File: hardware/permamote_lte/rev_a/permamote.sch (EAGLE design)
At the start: 115 parts, among them IC1 NRF9160, J1 TC2030-JLINK-NL, J2 U.FL-R-SMT, J3 NANO_SIM, J4 U.FL-R-SMT, J5 DM3AT-SF-PEJM5, Q1 PMDXB950UPEL, Q10 PMDXB950UPEL, Q2 PMDXB950UPEL, Q3 PMDXB950UPEL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

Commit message: cleaned up wirestubs
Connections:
- net GND: now also U13.EPAD
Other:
- moved on the sheet: TP30, TP31
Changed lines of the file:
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@@
 <part name="GND40" library="supply1" library_urn="urn:adsk.eagle:library:371" deviceset="GND" device=""/>
 <part name="P+13" library="supply1" library_urn="urn:adsk.eagle:library:371" deviceset="VCC" device=""/>
+<part name="GND41" library="umich" deviceset="GND" device=""/>
 </parts>
 <sheets>
@@
 <attribute name="AUTHOR" x="169.545" y="6.35" size="2.54" layer="94" font="vector"/>
 </instance>
-<instance part="TP30" gate="G$1" x="50.8" y="124.46" smashed="yes" rot="R270">
-<attribute name="NAME" x="50.8" y="127.635" size="1.016" layer="95" ratio="12" rot="R270" align="center-right"/>
-</instance>
-<instance part="TP31" gate="G$1" x="50.8" y="109.22" smashed="yes" rot="R90">
-<attribute name="NAME" x="50.8" y="106.045" size="1.016" layer="95" ratio="12" rot="R90" align="center-right"/>
+<instance part="TP30" gate="G$1" x="132.08" y="121.92" smashed="yes" rot="R270">
+<attribute name="NAME" x="132.08" y="125.095" size="1.016" layer="95" ratio="12" rot="R270" align="center-right"/>
+</instance>
+<instance part="TP31" gate="G$1" x="132.08" y="106.68" smashed="yes" rot="R90">
+<attribute name="NAME" x="132.08" y="103.505" size="1.016" layer="95" ratio="12" rot="R90" align="center-right"/>
 </instance>
 <instance part="TP32" gate="G$1" x="109.22" y="60.96" smashed="yes">
@@
 <instance part="P+13" gate="VCC" x="60.96" y="88.9" smashed="yes">
 <attribute name="VALUE" x="58.42" y="86.36" size="1.778" layer="96" rot="R90"/>
+</instance>
+<instance part="GND41" gate="1" x="50.8" y="104.14" smashed="yes">
+<attribute name="VALUE" x="48.26" y="101.6" size="1.778" layer="96"/>
 </instance>
 </instances>
@@
 <net name="SIM_1V8" class="0">
 <segment>
-<wire x1="129.54" y1="109.22" x2="137.16" y2="109.22" width="0.1524" layer="91"/>
-<label x="137.16" y="109.22" size="1.27" layer="95" xref="yes"/>
+<wire x1="53.34" y1="111.76" x2="48.26" y2="111.76" width="0.1524" layer="91"/>
+<label x="48.26" y="111.76" size="1.27" layer="95" rot="R180" xref="yes"/>
 <pinref part="U13" gate="A" pin="VCC"/>
 </segment>
@@
 <net name="SIM_CLK" class="0">
 <segment>
-<wire x1="129.54" y1="114.3" x2="137.16" y2="114.3" width="0.1524" layer="91"/>
-<label x="137.16" y="114.3" size="1.27" layer="95" xref="yes"/>
+<wire x1="53.34" y1="116.84" x2="48.26" y2="116.84" width="0.1524" layer="91"/>
+<label x="48.26" y="116.84" size="1.27" layer="95" rot="R180" xref="yes"/>
 <pinref part="U13" gate="A" pin="CLK_IN"/>
 </segment>
@@
 <net name="SIM_IO" class="0">
 <segment>
-<wire x1="129.54" y1="111.76" x2="137.16" y2="111.76" width="0.1524" layer="91"/>
-<label x="137.16" y="111.76" size="1.27" layer="95" xref="yes"/>
+<wire x1="53.34" y1="114.3" x2="48.26" y2="114.3" width="0.1524" layer="91"/>
+<label x="48.26" y="114.3" size="1.27" layer="95" rot="R180" xref="yes"/>
 <pinref part="U13" gate="A" pin="DATA2_IN"/>
 </segment>
@@
 <net name="SIM_RST2" class="0">
 <segment>
-<wire x1="53.34" y1="119.38" x2="50.8" y2="119.38" width="0.1524" layer="91"/>
-<label x="45.72" y="119.38" size="1.27" layer="95" rot="R180" xref="yes"/>
-<wire x1="50.8" y1="119.38" x2="45.72" y2="119.38" width="0.1524" layer="91"/>
-<wire x1="50.8" y1="121.92" x2="50.8" y2="119.38" width="0.1524" layer="91"/>
-<junction x="50.8" y="119.38"/>
+<wire x1="129.54" y1="116.84" x2="132.08" y2="116.84" width="0.1524" layer="91"/>
+<label x="134.62" y="116.84" size="1.27" layer="95" xref="yes"/>
+<wire x1="132.08" y1="116.84" x2="134.62" y2="116.84" width="0.1524" layer="91"/>
+<wire x1="132.08" y1="119.38" x2="132.08" y2="116.84" width="0.1524" layer="91"/>
+<junction x="132.08" y="116.84"/>
 <pinref part="TP30" gate="G$1" pin="TESTPOINT"/>
 <pinref part="U13" gate="A" pin="DATA1_OUT"/>
@@
 <net name="SIM_CLK2" class="0">
 <segment>
-<wire x1="53.34" y1="116.84" x2="45.72" y2="116.84" width="0.1524" layer="91"/>
-<label x="45.72" y="116.84" size="1.27" layer="95" rot="R180" xref="yes"/>
+<wire x1="129.54" y1="114.3" x2="134.62" y2="114.3" width="0.1524" layer="91"/>
+<label x="134.62" y="114.3" size="1.27" layer="95" xref="yes"/>
 <pinref part="U13" gate="A" pin="CLK_OUT"/>
 </segment>
@@
 <net name="SIM_IO2" class="0">
 <segment>
-<wire x1="53.34" y1="114.3" x2="50.8" y2="114.3" width="0.1524" layer="91"/>
-<label x="45.72" y="114.3" size="1.27" layer="95" rot="R180" xref="yes"/>
-<wire x1="50.8" y1="114.3" x2="45.72" y2="114.3" width="0.1524" layer="91"/>
-<wire x1="50.8" y1="114.3" x2="50.8" y2="111.76" width="0.1524" layer="91"/>
-<junction x="50.8" y="114.3"/>
+<wire x1="129.54" y1="111.76" x2="132.08" y2="111.76" width="0.1524" layer="91"/>
+<label x="134.62" y="111.76" size="1.27" layer="95" xref="yes"/>
+<wire x1="132.08" y1="111.76" x2="134.62" y2="111.76" width="0.1524" layer="91"/>
+<wire x1="132.08" y1="111.76" x2="132.08" y2="109.22" width="0.1524" layer="91"/>
+<junction x="132.08" y="111.76"/>
 <pinref part="TP31" gate="G$1" pin="TESTPOINT"/>
 <pinref part="U13" gate="A" pin="DATA2_OUT"/>
@@
 <net name="SIM_RST" class="0">
 <segment>
-<wire x1="129.54" y1="116.84" x2="137.16" y2="116.84" width="0.1524" layer="91"/>
-<label x="137.16" y="116.84" size="1.27" layer="95" xref="yes"/>
+<wire x1="53.34" y1="119.38" x2="48.26" y2="119.38" width="0.1524" layer="91"/>
+<label x="48.26" y="119.38" size="1.27" layer="95" rot="R180" xref="yes"/>
 <pinref part="U13" gate="A" pin="DATA1_IN"/>
 </segment>
@@
 <junction x="99.06" y="50.8"/>
 </segment>
-</net>
+<segment>
+<pinref part="U13" gate="A" pin="EPAD"/>
+<wire x1="53.34" y1="109.22" x2="50.8" y2="109.22" width="0.1524" layer="91"/>
+<pinref part="GND41" gate="1" pin="GND"/>
+<wire x1="50.8" y1="109.22" x2="50.8" y2="106.68" width="0.1524" layer="91"/>
+</segment>
+</net>

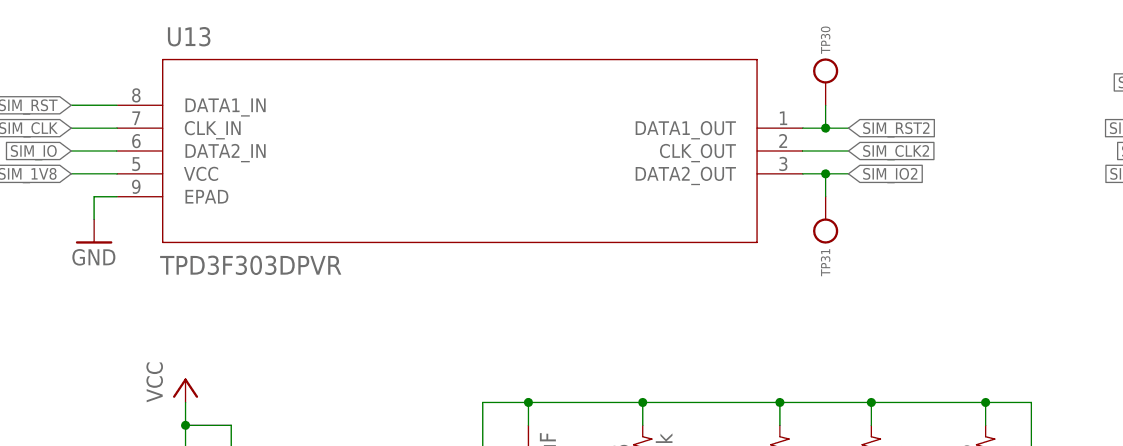
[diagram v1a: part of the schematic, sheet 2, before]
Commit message: replaced parts with correct library
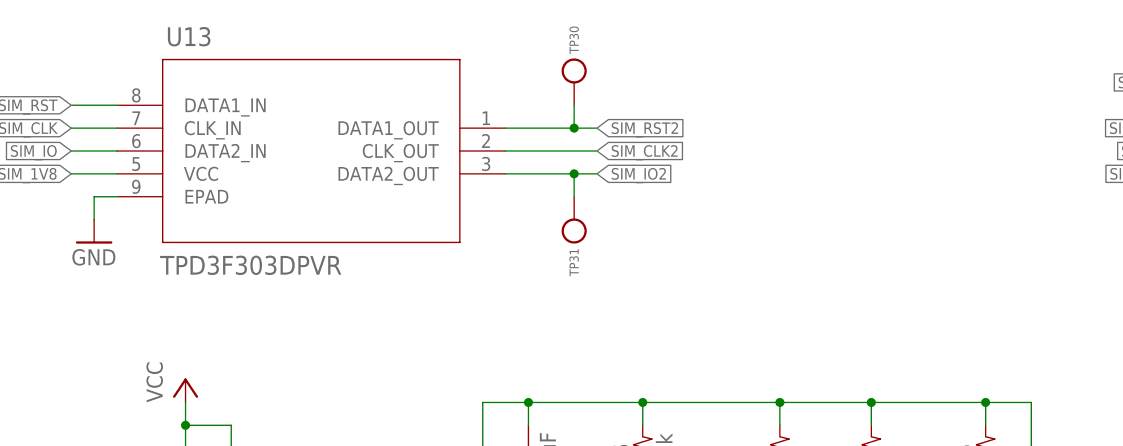
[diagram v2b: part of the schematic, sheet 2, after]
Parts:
- ANT1: device 1462350001:1462350001 -> chips:1462350001
- IC1: device nRF9160:NRF9160 -> chips:NRF9160
- U13: device TPD3F303:TPD3F303DPVR -> chips:TPD3F303DPVR
- U4: device Particle:BGA725L6 -> chips:BGA725L6
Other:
- moved on the sheet: TP30, TP31, U13
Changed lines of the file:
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@@
 <part name="J4" library="connector" deviceset="U.FL-R-SMT" device=""/>
 <part name="GND28" library="supply1" library_urn="urn:adsk.eagle:library:371" deviceset="GND" device=""/>
-<part name="ANT1" library="1462350001" deviceset="1462350001" device=""/>
+<part name="ANT1" library="chips" deviceset="1462350001" device=""/>
 <part name="BAT1" library="batteries" deviceset="2477THMCOINCELLCLIP" device=""/>
 <part name="GND32" library="supply1" library_urn="urn:adsk.eagle:library:371" deviceset="GND" device=""/>
-<part name="IC1" library="nRF9160" deviceset="NRF9160" device=""/>
+<part name="IC1" library="chips" deviceset="NRF9160" device=""/>
 <part name="C3" library="passives" deviceset="CAPACITOR" device="0402_CAP" value="DNP"/>
 <part name="C4" library="passives" deviceset="CAPACITOR" device="0402_CAP" value="DNP"/>
 <part name="GND33" library="supply1" library_urn="urn:adsk.eagle:library:371" deviceset="GND" device=""/>
-<part name="U4" library="Particle" deviceset="BGA725L6" device=""/>
+<part name="U4" library="chips" deviceset="BGA725L6" device=""/>
 <part name="L2" library="passives" deviceset="INDUCTOR" device="0402" value="5.1nH"/>
 <part name="L4" library="passives" deviceset="INDUCTOR" device="0402" value="1.8nH"/>
@@
 <part name="TP31" library="headers" deviceset="TEST-POINT" device=""/>
 <part name="TP32" library="headers" deviceset="TEST-POINT" device=""/>
-<part name="U13" library="TPD3F303" deviceset="TPD3F303DPVR" device=""/>
+<part name="U13" library="chips" deviceset="TPD3F303DPVR" device=""/>
 <part name="GND38" library="supply1" library_urn="urn:adsk.eagle:library:371" deviceset="GND" device=""/>
 <part name="GND39" library="supply1" library_urn="urn:adsk.eagle:library:371" deviceset="GND" device=""/>
@@
 <attribute name="AUTHOR" x="169.545" y="6.35" size="2.54" layer="94" font="vector"/>
 </instance>
-<instance part="TP30" gate="G$1" x="132.08" y="121.92" smashed="yes" rot="R270">
-<attribute name="NAME" x="132.08" y="125.095" size="1.016" layer="95" ratio="12" rot="R270" align="center-right"/>
-</instance>
-<instance part="TP31" gate="G$1" x="132.08" y="106.68" smashed="yes" rot="R90">
-<attribute name="NAME" x="132.08" y="103.505" size="1.016" layer="95" ratio="12" rot="R90" align="center-right"/>
+<instance part="TP30" gate="G$1" x="104.14" y="121.92" smashed="yes" rot="R270">
+<attribute name="NAME" x="104.14" y="125.095" size="1.016" layer="95" ratio="12" rot="R270" align="center-right"/>
+</instance>
+<instance part="TP31" gate="G$1" x="104.14" y="106.68" smashed="yes" rot="R90">
+<attribute name="NAME" x="104.14" y="103.505" size="1.016" layer="95" ratio="12" rot="R90" align="center-right"/>
 </instance>
 <instance part="TP32" gate="G$1" x="109.22" y="60.96" smashed="yes">
@@
 <net name="SIM_RST2" class="0">
 <segment>
-<wire x1="129.54" y1="116.84" x2="132.08" y2="116.84" width="0.1524" layer="91"/>
-<label x="134.62" y="116.84" size="1.27" layer="95" xref="yes"/>
-<wire x1="132.08" y1="116.84" x2="134.62" y2="116.84" width="0.1524" layer="91"/>
-<wire x1="132.08" y1="119.38" x2="132.08" y2="116.84" width="0.1524" layer="91"/>
-<junction x="132.08" y="116.84"/>
+<wire x1="96.52" y1="116.84" x2="104.14" y2="116.84" width="0.1524" layer="91"/>
+<label x="106.68" y="116.84" size="1.27" layer="95" xref="yes"/>
+<wire x1="104.14" y1="116.84" x2="106.68" y2="116.84" width="0.1524" layer="91"/>
+<wire x1="104.14" y1="119.38" x2="104.14" y2="116.84" width="0.1524" layer="91"/>
+<junction x="104.14" y="116.84"/>
 <pinref part="TP30" gate="G$1" pin="TESTPOINT"/>
 <pinref part="U13" gate="A" pin="DATA1_OUT"/>
@@
 <net name="SIM_CLK2" class="0">
 <segment>
-<wire x1="129.54" y1="114.3" x2="134.62" y2="114.3" width="0.1524" layer="91"/>
-<label x="134.62" y="114.3" size="1.27" layer="95" xref="yes"/>
+<wire x1="96.52" y1="114.3" x2="106.68" y2="114.3" width="0.1524" layer="91"/>
+<label x="106.68" y="114.3" size="1.27" layer="95" xref="yes"/>
 <pinref part="U13" gate="A" pin="CLK_OUT"/>
 </segment>
@@
 <net name="SIM_IO2" class="0">
 <segment>
-<wire x1="129.54" y1="111.76" x2="132.08" y2="111.76" width="0.1524" layer="91"/>
-<label x="134.62" y="111.76" size="1.27" layer="95" xref="yes"/>
-<wire x1="132.08" y1="111.76" x2="134.62" y2="111.76" width="0.1524" layer="91"/>
-<wire x1="132.08" y1="111.76" x2="132.08" y2="109.22" width="0.1524" layer="91"/>
-<junction x="132.08" y="111.76"/>
+<wire x1="96.52" y1="111.76" x2="104.14" y2="111.76" width="0.1524" layer="91"/>
+<label x="106.68" y="111.76" size="1.27" layer="95" xref="yes"/>
+<wire x1="104.14" y1="111.76" x2="106.68" y2="111.76" width="0.1524" layer="91"/>
+<wire x1="104.14" y1="111.76" x2="104.14" y2="109.22" width="0.1524" layer="91"/>
+<junction x="104.14" y="111.76"/>
 <pinref part="TP31" gate="G$1" pin="TESTPOINT"/>
 <pinref part="U13" gate="A" pin="DATA2_OUT"/>

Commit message: update 9160
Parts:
- renumbered IC1 to U5

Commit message: fixing labels and stuff
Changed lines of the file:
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@@
 <attribute name="VALUE" x="182.88" y="127" size="1.27" layer="96"/>
 </instance>
-<instance part="GND35" gate="1" x="180.34" y="114.3" smashed="yes">
-<attribute name="VALUE" x="177.8" y="111.76" size="1.778" layer="96"/>
+<instance part="GND35" gate="1" x="180.34" y="116.84" smashed="yes">
+<attribute name="VALUE" x="177.8" y="114.3" size="1.778" layer="96"/>
 </instance>
 <instance part="GND1" gate="1" x="142.24" y="152.4" smashed="yes">
@@
 <pinref part="GND35" gate="1" pin="GND"/>
 <pinref part="J2" gate="G$1" pin="P$2"/>
-<wire x1="180.34" y1="116.84" x2="180.34" y2="124.46" width="0.1524" layer="91"/>
+<wire x1="180.34" y1="119.38" x2="180.34" y2="124.46" width="0.1524" layer="91"/>
 </segment>
 <segment>
@@
 <net name="GPS_EN" class="0">
 <segment>
+<label x="149.86" y="111.76" size="1.27" layer="95" xref="yes"/>
+<pinref part="U5" gate="G$1" pin="MAGPIO0"/>
 <wire x1="144.78" y1="114.3" x2="147.32" y2="114.3" width="0.1524" layer="91"/>
-<label x="147.32" y="114.3" size="1.27" layer="95" xref="yes"/>
-<pinref part="U5" gate="G$1" pin="MAGPIO0"/>
-</segment>
-<segment>
+<wire x1="147.32" y1="114.3" x2="147.32" y2="111.76" width="0.1524" layer="91"/>
+<wire x1="147.32" y1="111.76" x2="149.86" y2="111.76" width="0.1524" layer="91"/>
+</segment>
+<segment>
